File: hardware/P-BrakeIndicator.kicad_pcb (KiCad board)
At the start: 2 copper layers, 33.5 x 25.5 mm, 13 parts, among them J1 -PRW+, J2 RX TX, J3 +SPK-, J4 Ir.In, Q1 2N7000, U1 ATtiny202

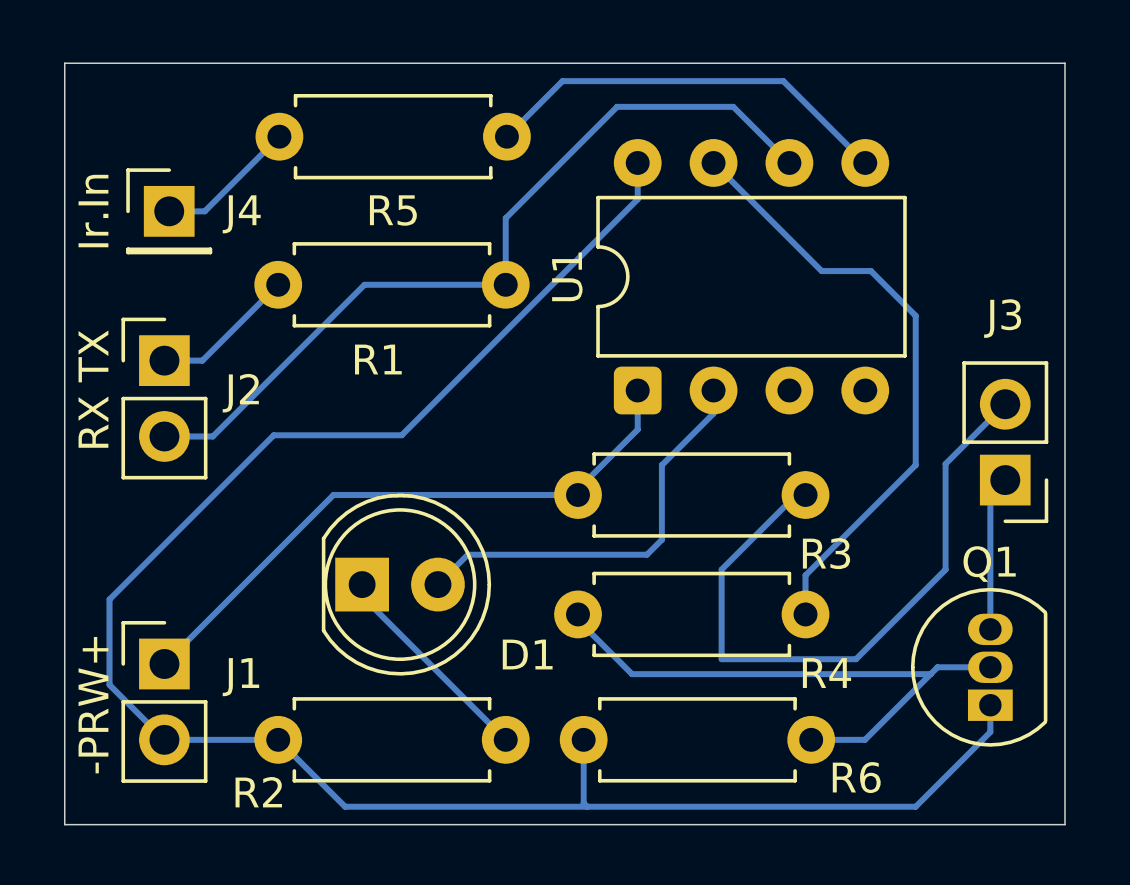
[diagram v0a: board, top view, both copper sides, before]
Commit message: pcb: widen power traces and relocate hardware project assets
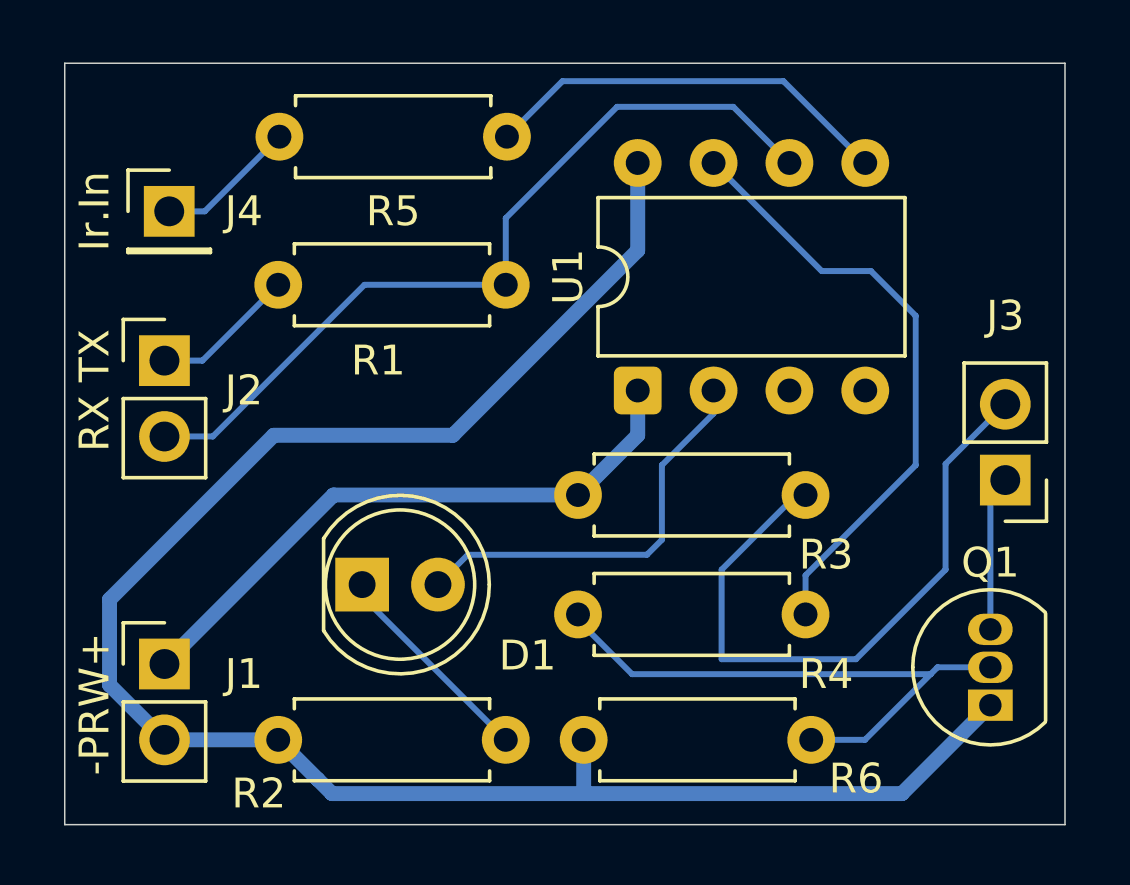
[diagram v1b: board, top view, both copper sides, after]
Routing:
- net +3.3V: track 21.2 -> 20.7 mm
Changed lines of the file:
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@@
 	)
 	(segment
-		(start 59 68)
-		(end 67.19 68)
-		(width 0.2)
-		(layer "B.Cu")
-		(net "+3.3V")
-	)
-	(segment
-		(start 67.19 67.81)
-		(end 69.19 65.81)
-		(width 0.2)
+		(start 69.19 64.5)
+		(end 69.19 66)
+		(width 0.5)
+		(layer "B.Cu")
+		(net "+3.3V")
+	)
+	(segment
+		(start 67.19 68)
+		(end 69.19 66)
+		(width 0.5)
+		(layer "B.Cu")
+		(net "+3.3V")
+	)
+	(segment
+		(start 67.19 68)
+		(end 59 68)
+		(width 0.5)
 		(layer "B.Cu")
 		(net "+3.3V")
@@
 		(start 53.34 73.66)
 		(end 59 68)
-		(width 0.2)
-		(layer "B.Cu")
-		(net "+3.3V")
-	)
-	(segment
-		(start 69.19 65.81)
-		(end 69.19 63.805)
-		(width 0.2)
+		(width 0.5)
 		(layer "B.Cu")
 		(net "+3.3V")
@@
 	)
 	(segment
+		(start 67.38 76.2)
+		(end 67.38 77.88)
+		(width 0.5)
+		(layer "B.Cu")
+		(net "GND")
+	)
+	(segment
+		(start 53.34 76.2)
+		(end 57.15 76.2)
+		(width 0.5)
+		(layer "B.Cu")
+		(net "GND")
+	)
+	(segment
+		(start 57.15 76.2)
+		(end 58.475 77.525)
+		(width 0.5)
+		(layer "B.Cu")
+		(net "GND")
+	)
+	(segment
 		(start 69.19 56.88)
-		(end 69.19 58.095635)
-		(width 0.2)
-		(layer "B.Cu")
-		(net "GND")
-	)
-	(segment
-		(start 57.15 76.2)
-		(end 59.39 78.44)
-		(width 0.2)
+		(end 69.19 59.81)
+		(width 0.5)
+		(layer "B.Cu")
+		(net "GND")
+	)
+	(segment
+		(start 67.38 77.88)
+		(end 67.5 78)
+		(width 0.2)
+		(layer "B.Cu")
+		(net "GND")
+	)
+	(segment
+		(start 67.5 78)
+		(end 78.04 78)
+		(width 0.5)
+		(layer "B.Cu")
+		(net "GND")
+	)
+	(segment
+		(start 57 66)
+		(end 51.5 71.5)
+		(width 0.5)
+		(layer "B.Cu")
+		(net "GND")
+	)
+	(segment
+		(start 67.19 76.08)
+		(end 67.31 76.2)
+		(width 0.2)
+		(layer "B.Cu")
+		(net "GND")
+	)
+	(segment
+		(start 51.5 74.36)
+		(end 53.34 76.2)
+		(width 0.5)
+		(layer "B.Cu")
+		(net "GND")
+	)
+	(segment
+		(start 78.04 78)
+		(end 81 75.04)
+		(width 0.5)
+		(layer "B.Cu")
+		(net "GND")
+	)
+	(segment
+		(start 58.95 78)
+		(end 67.5 78)
+		(width 0.5)
+		(layer "B.Cu")
+		(net "GND")
+	)
+	(segment
+		(start 63 66)
+		(end 57 66)
+		(width 0.5)
+		(layer "B.Cu")
+		(net "GND")
+	)
+	(segment
+		(start 69.19 59.81)
+		(end 63 66)
+		(width 0.5)
 		(layer "B.Cu")
 		(net "GND")
@@
 		(start 51.5 71.5)
 		(end 51.5 74.36)
-		(width 0.2)
-		(layer "B.Cu")
-		(net "GND")
-	)
-	(segment
-		(start 53.34 76.2)
-		(end 57.15 76.2)
-		(width 0.2)
-		(layer "B.Cu")
-		(net "GND")
-	)
-	(segment
-		(start 59.39 78.44)
-		(end 67.5 78.44)
-		(width 0.2)
-		(layer "B.Cu")
-		(net "GND")
-	)
-	(segment
-		(start 61.285635 66)
-		(end 57 66)
-		(width 0.2)
-		(layer "B.Cu")
-		(net "GND")
-	)
-	(segment
-		(start 67.38 76.2)
-		(end 67.38 78.32)
-		(width 0.2)
-		(layer "B.Cu")
-		(net "GND")
-	)
-	(segment
-		(start 67.19 76.08)
-		(end 67.31 76.2)
-		(width 0.2)
-		(layer "B.Cu")
-		(net "GND")
-	)
-	(segment
-		(start 78.5 78.44)
-		(end 81 75.94)
-		(width 0.2)
-		(layer "B.Cu")
-		(net "GND")
-	)
-	(segment
-		(start 67.5 78.44)
-		(end 78.5 78.44)
-		(width 0.2)
-		(layer "B.Cu")
-		(net "GND")
-	)
-	(segment
-		(start 67.38 78.32)
-		(end 67.5 78.44)
-		(width 0.2)
-		(layer "B.Cu")
-		(net "GND")
-	)
-	(segment
-		(start 81 75.94)
-		(end 81 75.04)
-		(width 0.2)
-		(layer "B.Cu")
-		(net "GND")
-	)
-	(segment
-		(start 69.19 58.095635)
-		(end 61.285635 66)
-		(width 0.2)
-		(layer "B.Cu")
-		(net "GND")
-	)
-	(segment
-		(start 57 66)
-		(end 51.5 71.5)
-		(width 0.2)
-		(layer "B.Cu")
-		(net "GND")
-	)
-	(segment
-		(start 51.5 74.36)
-		(end 53.34 76.2)
-		(width 0.2)
-		(layer "B.Cu")
-		(net "GND")
+		(width 0.5)
+		(layer "B.Cu")
+		(net "GND")
+	)
+	(segment
+		(start 58.475 77.525)
+		(end 58.95 78)
+		(width 0.5)
+		(layer "B.Cu")
+		(net "GND")

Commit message: pcb: update component values and increase track widths to 0.5mm
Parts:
- R3: value 0.1k -> 50Ω
- R4: value 10.Om -> 10Ω
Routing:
- net Net-(J3-Pin_2): track 22.0 -> 8.26 mm
- net Net-(U1-PA3): track 20.7 -> 27.0 mm
- net Net-(J2-Pin_2): track 27.8 -> 27.3 mm
- net Net-(U1-PA2): track 13.9 -> 13.4 mm
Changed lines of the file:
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@@
 			)
 		)
-		(property "Value" "0.1k"
+		(property "Value" "50Ω"
 			(at 5.19 0.12 0)
 			(layer "F.Fab")
@@
 			)
 		)
-		(property "Value" "10.Om"
+		(property "Value" "10Ω"
 			(at 4.81 0 0)
 			(layer "F.Fab")
@@
 		(start 81 72.5)
 		(end 81 68)
-		(width 0.2)
+		(width 0.5)
 		(layer "B.Cu")
 		(net "Net-(J3-Pin_1)")
@@
 	)
 	(segment
-		(start 76.5 73.5)
-		(end 79.5 70.5)
-		(width 0.2)
+		(start 78.46 68)
+		(end 81.5 64.96)
+		(width 0.5)
 		(layer "B.Cu")
 		(net "Net-(J3-Pin_2)")
@@
 	)
 	(segment
-		(start 72 73.5)
-		(end 76.5 73.5)
-		(width 0.2)
-		(layer "B.Cu")
-		(net "Net-(J3-Pin_2)")
-	)
-	(segment
-		(start 74.5 68)
-		(end 72 70.5)
-		(width 0.2)
-		(layer "B.Cu")
-		(net "Net-(J3-Pin_2)")
-	)
-	(segment
-		(start 79.5 66.96)
-		(end 81.5 64.96)
-		(width 0.2)
-		(layer "B.Cu")
-		(net "Net-(J3-Pin_2)")
-	)
-	(segment
-		(start 79.5 70.5)
-		(end 79.5 66.96)
-		(width 0.2)
-		(layer "B.Cu")
-		(net "Net-(J3-Pin_2)")
-	)
-	(segment
-		(start 72 70.5)
-		(end 72 73.5)
-		(width 0.2)
+		(start 74.81 68)
+		(end 78.46 68)
+		(width 0.5)
 		(layer "B.Cu")
 		(net "Net-(J3-Pin_2)")
@@
 		(start 54.61 63.5)
 		(end 57.15 60.96)
-		(width 0.2)
+		(width 0.5)
 		(layer "B.Cu")
 		(net "Net-(J2-Pin_1)")
@@
 		(start 53.34 63.5)
 		(end 54.61 63.5)
-		(width 0.2)
+		(width 0.5)
 		(layer "B.Cu")
 		(net "Net-(J2-Pin_1)")
+	)
+	(segment
+		(start 68.27 55.5)
+		(end 72.89 55.5)
+		(width 0.5)
+		(layer "B.Cu")
+		(net "Net-(J2-Pin_2)")
 	)
 	(segment
 		(start 60.04 60.96)
 		(end 64.77 60.96)
-		(width 0.2)
+		(width 0.5)
 		(layer "B.Cu")
 		(net "Net-(J2-Pin_2)")
 	)
 	(segment
-		(start 74.27 56.88)
-		(end 72.39 55)
-		(width 0.2)
+		(start 64.77 59)
+		(end 64.77 60.96)
+		(width 0.5)
 		(layer "B.Cu")
 		(net "Net-(J2-Pin_2)")
 	)
 	(segment
-		(start 64.77 58.73)
-		(end 68.5 55)
-		(width 0.2)
-		(layer "B.Cu")
-		(net "Net-(J2-Pin_2)")
-	)
-	(segment
-		(start 64.77 60.96)
-		(end 64.77 58.73)
-		(width 0.2)
+		(start 72.89 55.5)
+		(end 74.27 56.88)
+		(width 0.5)
 		(layer "B.Cu")
 		(net "Net-(J2-Pin_2)")
@@
 		(start 53.34 66.04)
 		(end 54.96 66.04)
-		(width 0.2)
+		(width 0.5)
 		(layer "B.Cu")
 		(net "Net-(J2-Pin_2)")
@@
 		(start 54.96 66.04)
 		(end 60.04 60.96)
-		(width 0.2)
+		(width 0.5)
 		(layer "B.Cu")
 		(net "Net-(J2-Pin_2)")
 	)
 	(segment
-		(start 68.5 55)
-		(end 72.39 55)
-		(width 0.2)
+		(start 64.77 59)
+		(end 68.27 55.5)
+		(width 0.5)
 		(layer "B.Cu")
 		(net "Net-(J2-Pin_2)")
@@
 		(start 54.69 58.5)
 		(end 57.19 56)
-		(width 0.2)
+		(width 0.5)
 		(layer "B.Cu")
 		(net "Net-(J4-Pin_1)")
@@
 		(start 53.5 58.5)
 		(end 54.69 58.5)
-		(width 0.2)
+		(width 0.5)
 		(layer "B.Cu")
 		(net "Net-(J4-Pin_1)")
@@
 		(start 70 67)
 		(end 71.73 65.27)
-		(width 0.2)
+		(width 0.5)
 		(layer "B.Cu")
 		(net "Net-(D1-A)")
@@
 		(start 62.5 71)
 		(end 63.5 70)
-		(width 0.2)
+		(width 0.5)
 		(layer "B.Cu")
 		(net "Net-(D1-A)")
@@
 		(start 69.5 70)
 		(end 70 69.5)
-		(width 0.2)
+		(width 0.5)
 		(layer "B.Cu")
 		(net "Net-(D1-A)")
@@
 		(start 63.5 70)
 		(end 69.5 70)
-		(width 0.2)
+		(width 0.5)
 		(layer "B.Cu")
 		(net "Net-(D1-A)")
@@
 		(start 70 69.5)
 		(end 70 67)
-		(width 0.2)
+		(width 0.5)
 		(layer "B.Cu")
 		(net "Net-(D1-A)")
 	)
 	(segment
-		(start 74.07 54.14)
-		(end 66.67 54.14)
-		(width 0.2)
+		(start 66.01 54.8)
+		(end 74.73 54.8)
+		(width 0.5)
 		(layer "B.Cu")
 		(net "Net-(U1-PA2)")
 	)
 	(segment
-		(start 76.81 56.88)
-		(end 74.07 54.14)
-		(width 0.2)
+		(start 74.73 54.8)
+		(end 76.81 56.88)
+		(width 0.5)
 		(layer "B.Cu")
 		(net "Net-(U1-PA2)")
 	)
 	(segment
-		(start 66.67 54.14)
-		(end 64.81 56)
-		(width 0.2)
+		(start 64.81 56)
+		(end 66.01 54.8)
+		(width 0.5)
 		(layer "B.Cu")
 		(net "Net-(U1-PA2)")
+	)
+	(segment
+		(start 78 58.5)
+		(end 79 59.5)
+		(width 0.5)
+		(layer "B.Cu")
+		(net "Net-(U1-PA3)")
 	)
 	(segment
@@
 	)
 	(segment
-		(start 78.5 67)
-		(end 74.81 70.69)
-		(width 0.2)
+		(start 79 59.5)
+		(end 79 65)
+		(width 0.5)
 		(layer "B.Cu")
 		(net "Net-(U1-PA3)")
 	)
 	(segment
-		(start 78.5 62)
-		(end 78.5 67)
-		(width 0.2)
+		(start 73 66.5)
+		(end 73 70.19)
+		(width 0.5)
+		(layer "B.Cu")
+		(net "Net-(U1-PA3)")
+	)
+	(segment
+		(start 71.73 56.88)
+		(end 73.35 58.5)
+		(width 0.5)
 		(layer "B.Cu")
 		(net "Net-(U1-PA3)")
@@
 	)
 	(segment
-		(start 74.81 70.69)
+		(start 73 70.19)
 		(end 74.81 72)
-		(width 0.2)
+		(width 0.5)
 		(layer "B.Cu")
 		(net "Net-(U1-PA3)")
 	)
 	(segment
-		(start 71.73 56.88)
-		(end 75.35 60.5)
-		(width 0.2)
+		(start 73.35 58.5)
+		(end 78 58.5)
+		(width 0.5)
 		(layer "B.Cu")
 		(net "Net-(U1-PA3)")
 	)
 	(segment
-		(start 75.35 60.5)
-		(end 77 60.5)
-		(width 0.2)
+		(start 79 65)
+		(end 77.5 66.5)
+		(width 0.5)
+		(layer "B.Cu")
+		(net "Net-(U1-PA3)")
+	)
+	(segment
+		(start 77.5 66.5)
+		(end 73 66.5)
+		(width 0.5)
 		(layer "B.Cu")
 		(net "Net-(U1-PA3)")
@@
 	)
 	(segment
-		(start 77 60.5)
-		(end 78.5 62)
-		(width 0.2)
-		(layer "B.Cu")
-		(net "Net-(U1-PA3)")
+		(start 69.19 59.81)
+		(end 66.5 62.5)
+		(width 0.5)
+		(layer "B.Cu")
+		(net "GND")
 	)
 	(segment
@@
 	)
 	(segment
+		(start 51.5 71.5)
+		(end 51.5 74.36)
+		(width 0.5)
+		(layer "B.Cu")
+		(net "GND")
+	)
+	(segment
 		(start 53.34 76.2)
 		(end 57.15 76.2)
@@
 	)
 	(segment
-		(start 69.19 56.88)
-		(end 69.19 59.81)
+		(start 51.5 74.36)
+		(end 53.34 76.2)
 		(width 0.5)
 		(layer "B.Cu")
@@
 	)
 	(segment
+		(start 60.5 62.5)
+		(end 51.5 71.5)
+		(width 0.5)
+		(layer "B.Cu")
+		(net "GND")
+	)
+	(segment
 		(start 67.5 78)
 		(end 78.04 78)
-		(width 0.5)
-		(layer "B.Cu")
-		(net "GND")
-	)
-	(segment
-		(start 57 66)
-		(end 51.5 71.5)
 		(width 0.5)
 		(layer "B.Cu")
@@
 	)
 	(segment
-		(start 51.5 74.36)
-		(end 53.34 76.2)
-		(width 0.5)
-		(layer "B.Cu")
-		(net "GND")
-	)
-	(segment
 		(start 78.04 78)
 		(end 81 75.04)
@@
 	)
 	(segment
-		(start 63 66)
-		(end 57 66)
+		(start 66.5 62.5)
+		(end 60.5 62.5)
 		(width 0.5)
 		(layer "B.Cu")
@@
 	)
 	(segment
-		(start 69.19 59.81)
-		(end 63 66)
-		(width 0.5)
-		(layer "B.Cu")
-		(net "GND")
-	)
-	(segment
-		(start 51.5 71.5)
-		(end 51.5 74.36)
+		(start 69.19 56.88)
+		(end 69.19 59.81)
 		(width 0.5)
 		(layer "B.Cu")
@@
 		(start 60 71.43)
 		(end 64.77 76.2)
-		(width 0.2)
+		(width 0.5)
 		(layer "B.Cu")
 		(net "Net-(D1-K)")
@@
 		(start 67 72)
 		(end 69 74)
-		(width 0.2)
+		(width 0.5)
 		(layer "B.Cu")
 		(net "Net-(Q1-G)")
@@
 		(start 79.23 73.77)
 		(end 81 73.77)
-		(width 0.2)
+		(width 0.5)
 		(layer "B.Cu")
 		(net "Net-(Q1-G)")
@@
 		(start 75 76.2)
 		(end 76.8 76.2)
-		(width 0.2)
+		(width 0.5)
 		(layer "B.Cu")
 		(net "Net-(Q1-G)")
@@
 		(start 76.8 76.2)
 		(end 79 74)
-		(width 0.2)
+		(width 0.5)
 		(layer "B.Cu")
 		(net "Net-(Q1-G)")
@@
 		(start 79 74)
 		(end 79.23 73.77)
-		(width 0.2)
+		(width 0.5)
 		(layer "B.Cu")
 		(net "Net-(Q1-G)")
@@
 		(start 69 74)
 		(end 79 74)
-		(width 0.2)
+		(width 0.5)
 		(layer "B.Cu")
 		(net "Net-(Q1-G)")

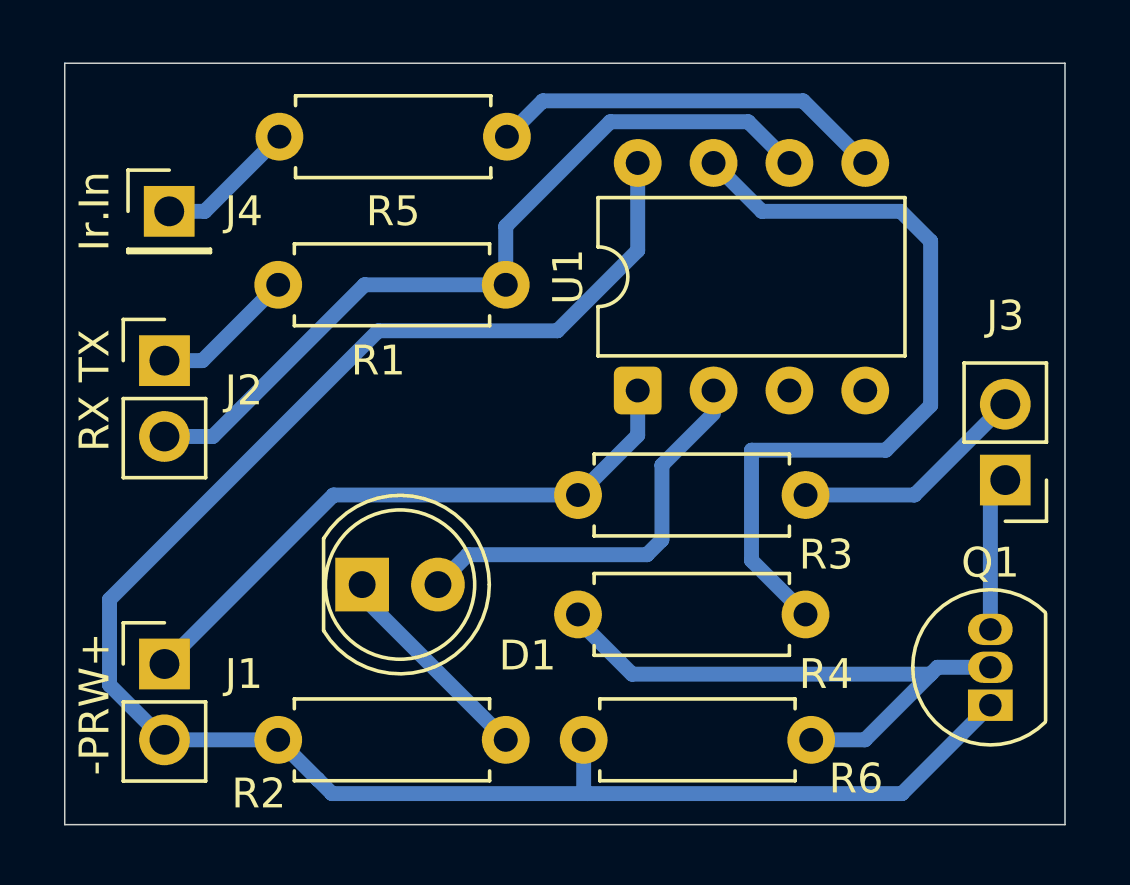
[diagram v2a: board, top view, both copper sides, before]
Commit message: refactor: redesign board for comparator and carrier frequency
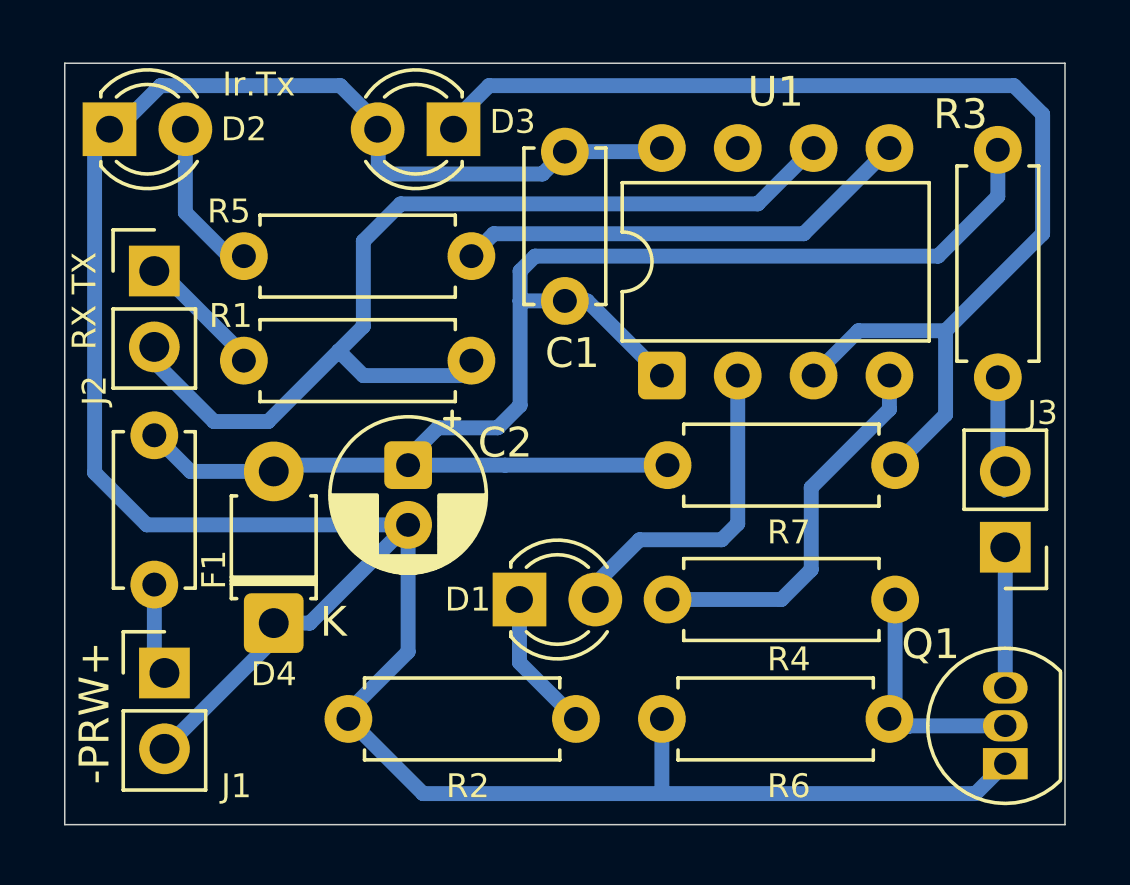
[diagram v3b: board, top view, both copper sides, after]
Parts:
- removed J4: Ir.In, Connector_PinHeader_2.54mm:PinHeader_1x01_P2.54mm_Vertical
- added C1: 0.1 uF, Capacitor_THT:C_Disc_D5.0mm_W2.5mm_P5.00mm, F.Cu at (66.8, 56.5)
- added C2: 220uF, Capacitor_THT:CP_Radial_D5.0mm_P2.00mm, F.Cu at (61.5, 67.0)
- added D2: Ir.Tx, LED_THT:LED_D3.0mm, F.Cu at (51.5, 55.8)
- added D3: Ir.Rx, LED_THT:LED_D3.0mm, F.Cu at (63.0, 55.8)
- added D4: P6KE5.6CA, Diode_THT:D_T-1_P5.08mm_Horizontal, F.Cu at (57.0, 72.3)
- added F1: Polyfuse, Capacitor_THT:C_Disc_D5.0mm_W2.5mm_P5.00mm, F.Cu at (53.0, 71.0)
- added R7: 10k, Resistor_THT:R_Axial_DIN0207_L6.3mm_D2.5mm_P7.62mm_Horizontal, F.Cu at (77.8, 67.0)
- D1: footprint LED_THT:LED_D5.0mm -> LED_THT:LED_D3.0mm
- R3: value 50Ω -> 20Ω
- R5: value 1k -> 510Ω
- moved R3 18.2 mm to (81.2, 56.4), turned to -90 degrees
- moved R5 9.68 mm to (56.0, 60.0), turned to 0 degrees
- moved D1 5.29 mm to (65.2, 71.5)
- moved R4 4.65 mm to (70.2, 71.5), turned to 0 degrees
- moved J2 3.02 mm to (53.0, 60.5)
- moved R1 2.79 mm to (56.0, 63.5)
- moved R6 2.71 mm to (77.6, 75.5)
- moved R2 2.45 mm to (59.5, 75.5)
- moved J3 2.25 mm to (81.5, 69.8)
- moved Q1 2.02 mm to (81.5, 77.0)
- moved U1 0.95 mm to (70.0, 64.0)
- moved J1 0.30 mm to (53.3, 74.0)
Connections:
- J1 pad 1: +3.3V -> +5V
- R3 pad 1: +3.3V -> Net-(D4-A2)
- R4 pad 1: Net-(U1-PA3) -> Net-(U1-PA1)
- R5 pad 1: Net-(U1-PA2) -> Net-(D2-A)
- R5 pad 2: Net-(J4-Pin_1) -> Net-(U1-PA2)
- U1 pad 1: +3.3V -> Net-(D4-A2)
- U1 pad 3: unconnected-(U1-PA7-Pad3) -> Net-(D3-K)
- U1 pad 4: unconnected-(U1-PA1-Pad4) -> Net-(U1-PA1)
- U1 pad 7: Net-(U1-PA3) -> unconnected-(U1-PA3-Pad7)
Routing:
- net Net-(D4-A2): track 0.00 -> 52.5 mm
- net Net-(D3-K): track 0.00 -> 40.2 mm
- net GND: track 62.6 -> 91.3 mm
- net Net-(U1-PA3): track 27.0 -> 0.00 mm
- net +3.3V: track 20.7 -> 0.00 mm
- net Net-(U1-PA1): track 0.00 -> 13.4 mm
- net Net-(Q1-G): track 20.3 -> 8.11 mm
- net Net-(J2-Pin_2): track 27.3 -> 33.5 mm
- net Net-(D2-A): track 0.00 -> 5.56 mm
- net Net-(J4-Pin_1): track 4.73 -> 0.00 mm
- net Net-(J3-Pin_2): track 8.26 -> 3.66 mm
- net +5V: track 0.00 -> 3.47 mm
- net Net-(D1-A): track 14.5 -> 11.1 mm
- net Net-(D1-K): track 7.22 -> 4.78 mm
- net Net-(U1-PA2): track 13.4 -> 15.5 mm
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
